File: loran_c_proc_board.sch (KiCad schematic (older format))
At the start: 0 parts

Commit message: Almost done: SPI, Relay optocouplers, ADC & DAC interface However, bug needs to be fixed: buses are not connected between hierarchical sheets
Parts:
- added BT101: Li CR2032, symbol BATTERY
- added C101: 470u 16V LowE, symbol CP1
- added C102, C105, C106, C108, C109: 100n, symbol C
- added C103, C107: 10u 6.3V Ta, symbol CP1
- added C104: 470u 6.3V, symbol CP1
- added D101: SMLVT3V3, symbol ZENER
- added FB101, FB102: Bead, symbol FILTER
- added P101: Power, symbol CONN_4X2
- added P102: Cortex SWD, symbol CONN_5X2
- added P103: Clock board, symbol CONN_5X2
- added R101: 100k, symbol R
- added R102: 33, symbol R
- added R103, R104, R105: 10, symbol R
- added R106, R107: 200, symbol R
- added U101: LD1117S33, symbol NCP1117ST33T3G
- added U102, U103: 74AC14, symbol 74HC14
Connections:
- net labels added: +15V, +5V, -15V, BPPS, BPROG, BSWD, CB_OSC, CB_PO1, CB_PO2, CB_PPS, NTRST, PPS3, PROG_OUT1, PROG_OUT2, SWCLK, SWDIO
- net labels removed: +3.3VADC, +5VA
- wire segments 0 -> 127
- no-connect marks 0 -> 4
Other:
- note added: "KEY"
- note added: "Place close to R? and P?"
- note added: "VDD"

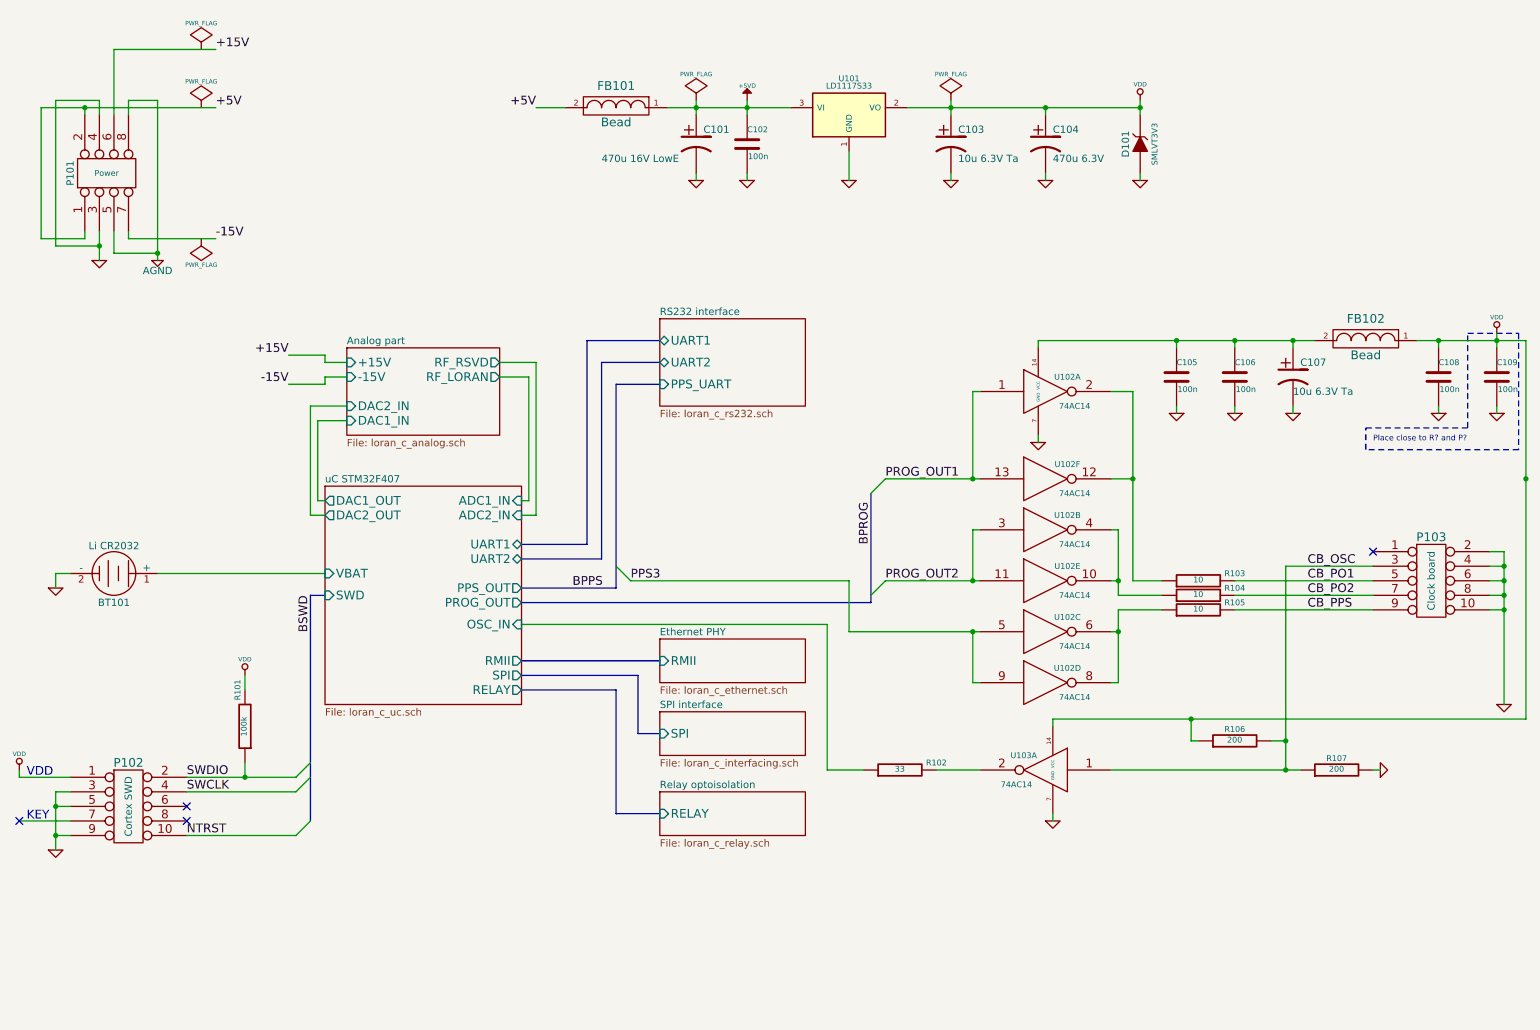
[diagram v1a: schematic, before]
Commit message: FIXED: no more buses on hierarchical sheet ports
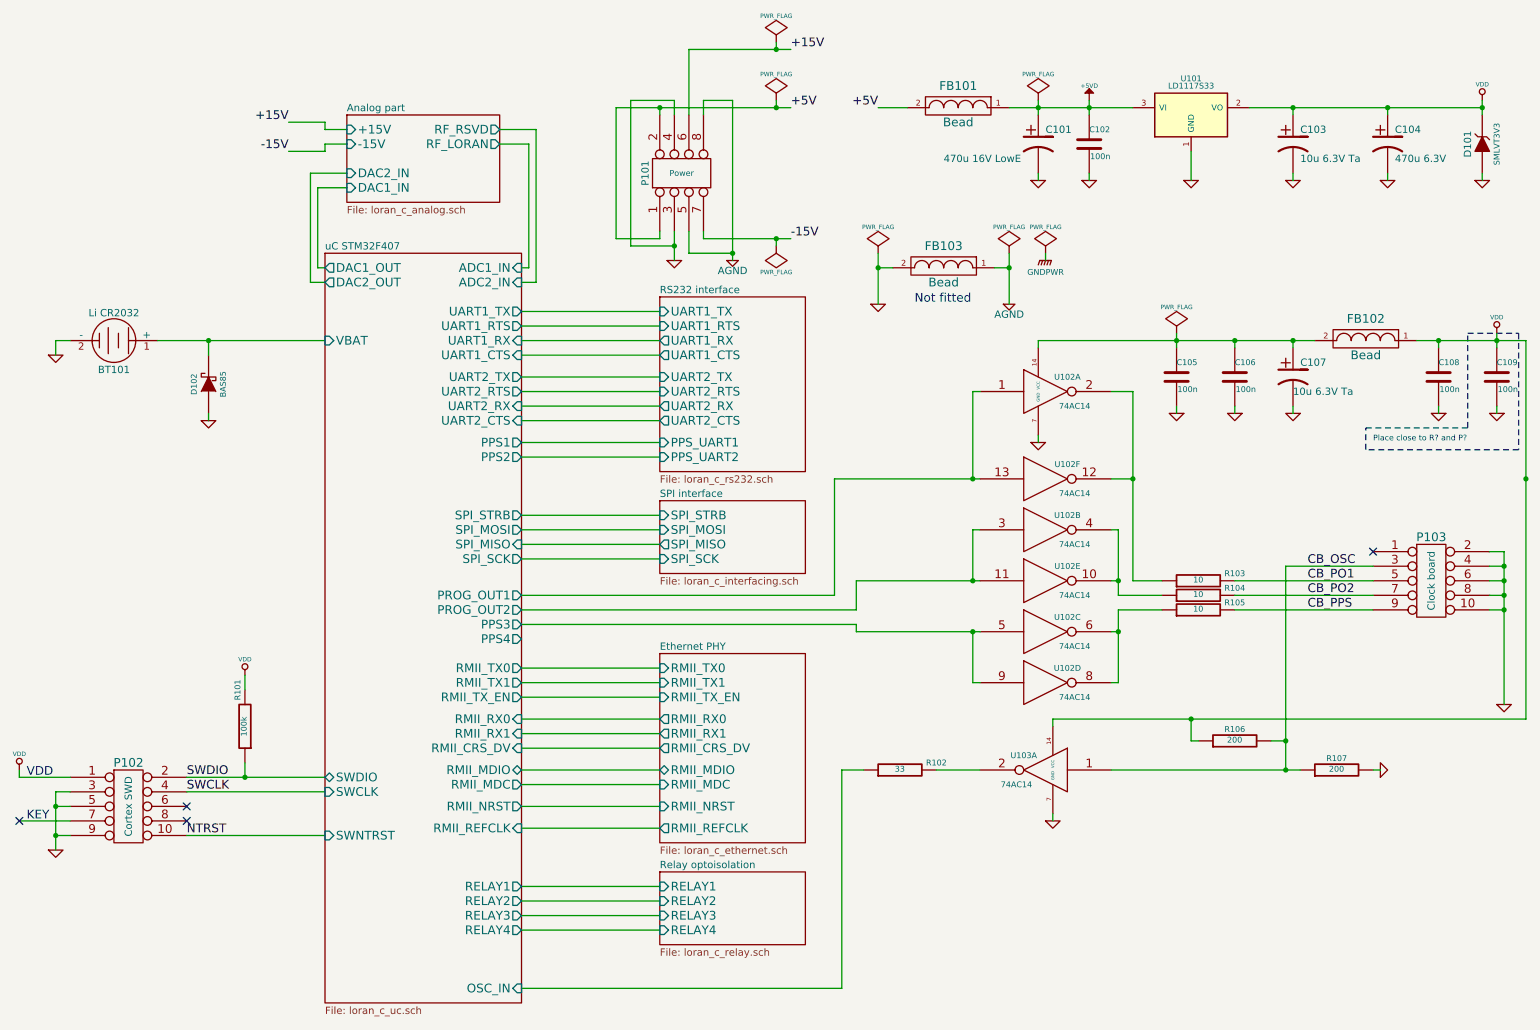
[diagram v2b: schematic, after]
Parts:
- added D102: BAS85, symbol DIODESCH
- added FB103: Bead, symbol FILTER
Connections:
- net AGND: now also FB103.1
- net GND: now also D102.1 (A), FB103.2
- net uC STM32F407/VBAT: now also D102.2 (K)
- net PPS3 renamed uC STM32F407/PPS3
- net PROG_OUT1 renamed uC STM32F407/PROG_OUT1
- net PROG_OUT2 renamed uC STM32F407/PROG_OUT2
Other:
- note added: "Not fitted"
- moved on the sheet: BT101, C101, C102, C103, C104, D101, FB101, P101, U101

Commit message: Update: fix, assign modules to components -Fix P302 incorrect connection -Assign footprints to components (not all yet) -Back-import footprints into schematic fields
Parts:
- C101: footprint (none) -> w_pth_capacitors:CP_10x12.5mm
- C102, C105, C106, C108, C109: footprint (none) -> w_smd_capacitors:c_1206
- C103, C107: footprint (none) -> w_smd_capacitors:c_tant_B
- C104: footprint (none) -> w_pth_capacitors:CP_6.3x11mm
- D101: footprint (none) -> w_smd_diode:do214aa
- D102: footprint (none) -> w_smd_diode:sod80c
- FB101, FB102, FB103: footprint (none) -> w_pth_resistors:RC07
- P102, P103: footprint (none) -> w_conn_strip:vasch_strip_5x2
- R101, R102, R103, R104, R105, R106, R107: footprint (none) -> w_smd_resistors:r_1206
- U101: footprint (none) -> SMD_Packages:SOT223
- U102, U103: footprint (none) -> w_smd_dil:so-16
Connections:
- net CB_OSC: now also R107.2; no longer R107.1
- net GND: now also R107.1; no longer R107.2
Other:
- note removed: "Place close to R? and P?"
- moved on the sheet: C109, R102, R106, R107, U103A

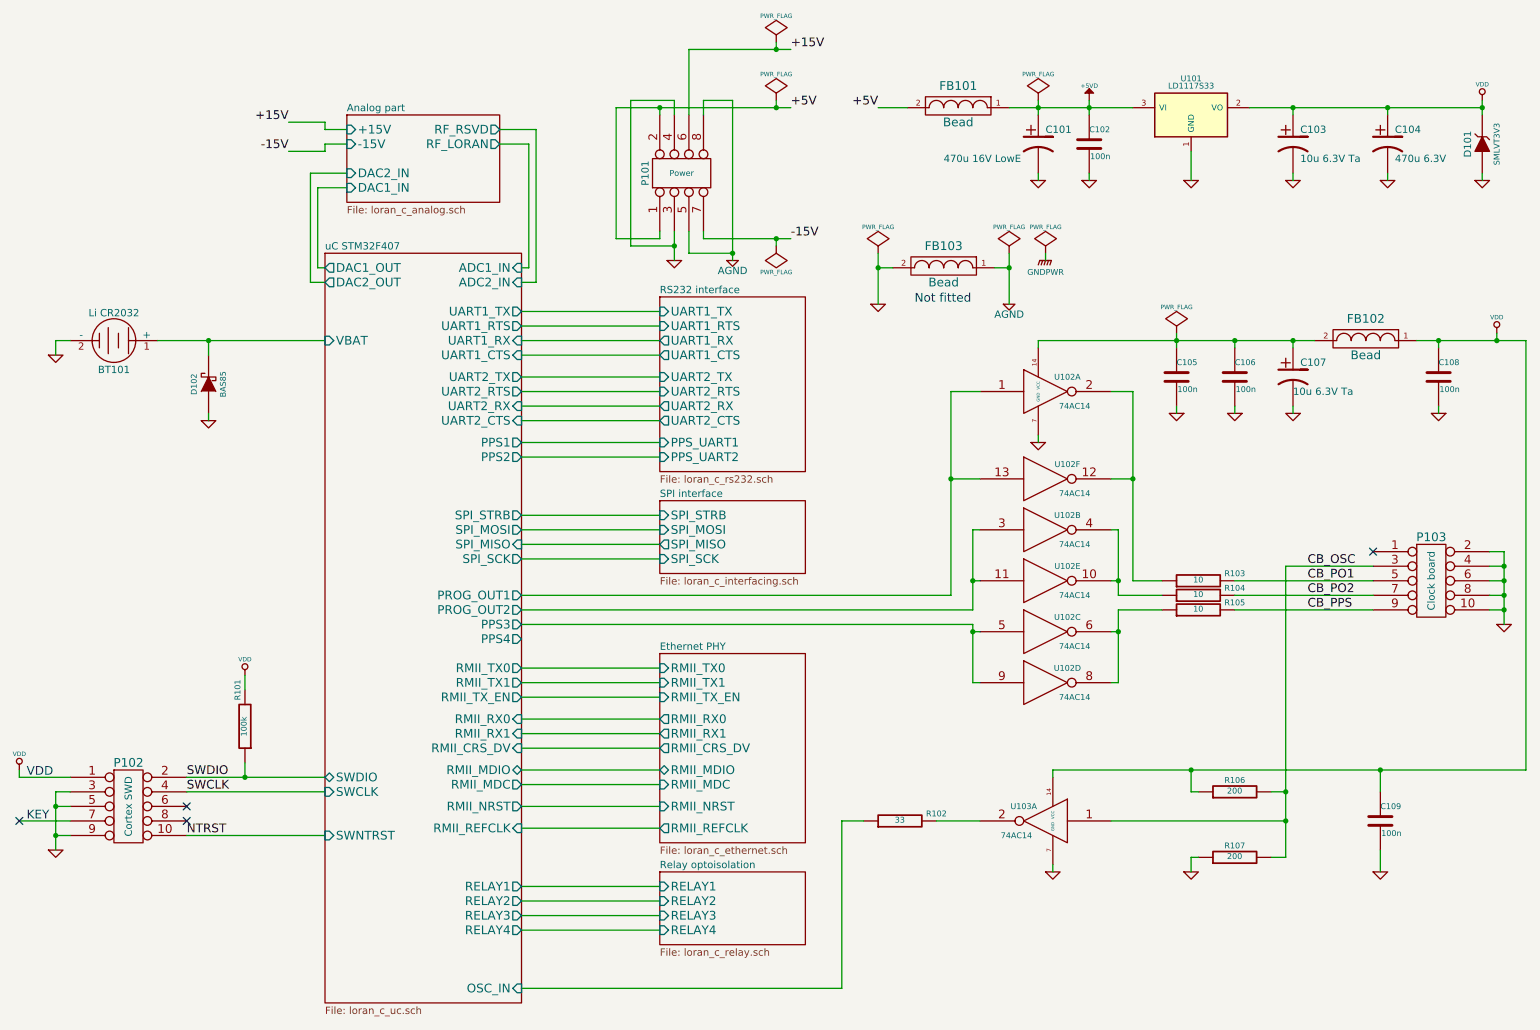
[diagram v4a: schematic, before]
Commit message: Update: assign footprint to P101, fix mounting hole symbol (pin # missing)
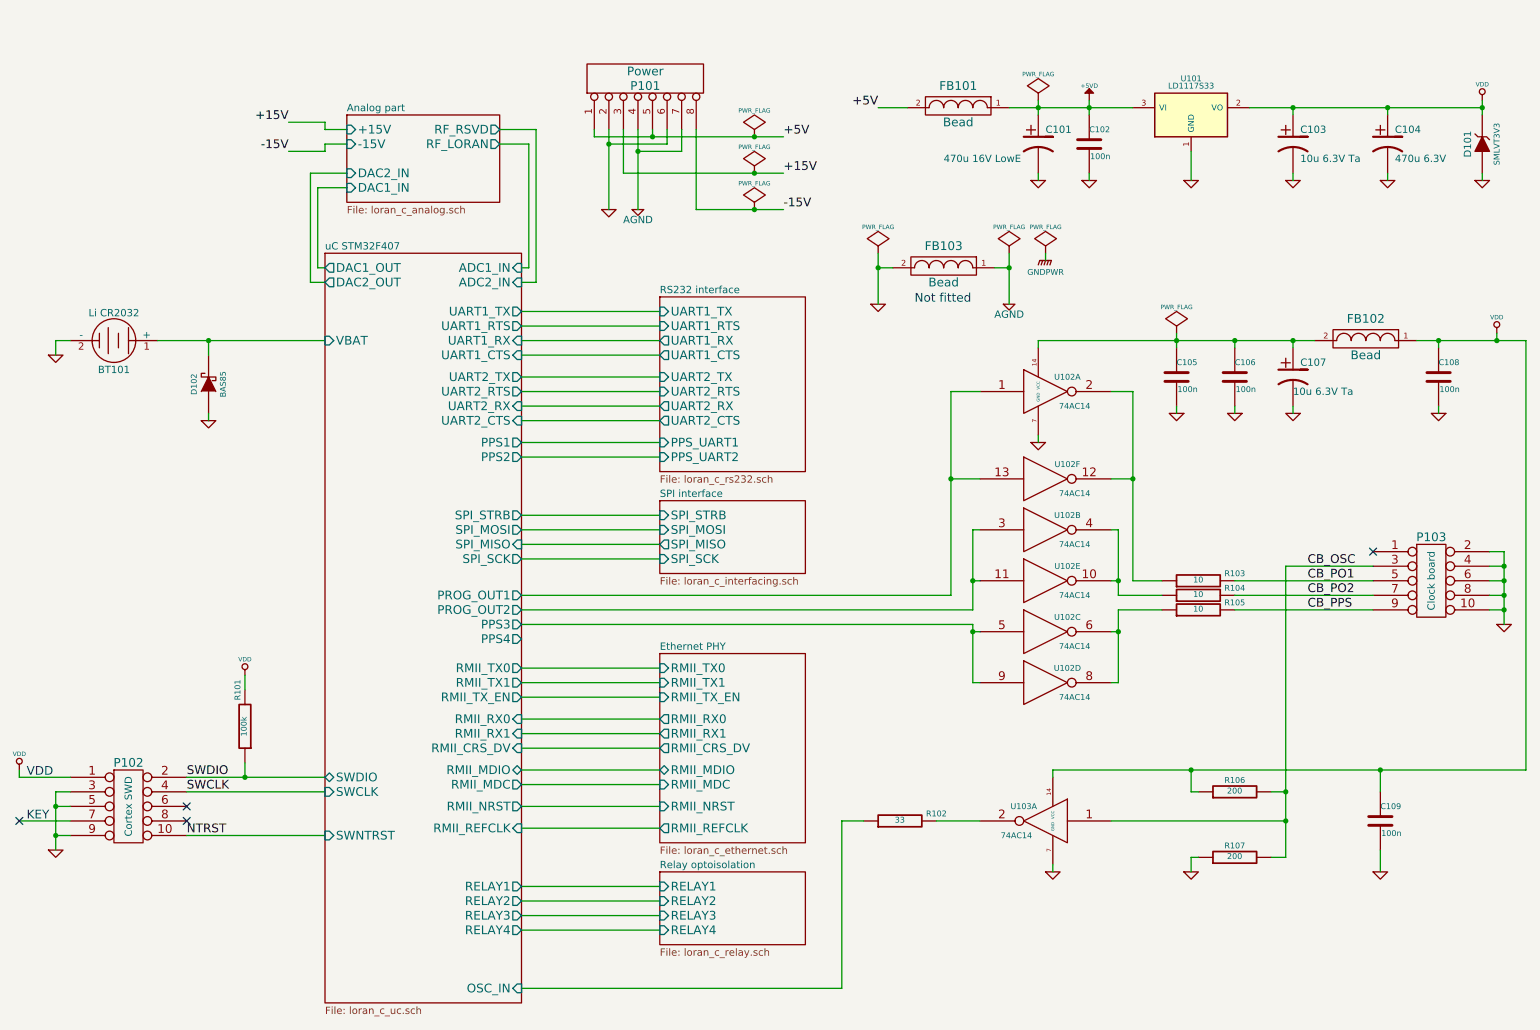
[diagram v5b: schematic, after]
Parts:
- removed P101: Power, symbol CONN_4X2
- added P101: Power, symbol CONN_8
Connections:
- net +15V: now also P101.3 (P3)
- net +5V: now also P101.1 (P1), P101.5 (P5)
- net -15V: now also P101.8 (P8)
- net AGND: now also P101.4 (P4), P101.7 (P7)
- net GND: now also P101.2 (P2), P101.6 (P6)

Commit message: Update: minor schematic rework (due to PCB routing), PCB routing in early stage
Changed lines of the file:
@@
 	8250 4750 8300 4750
 Wire Wire Line
-	8300 4600 8300 4750
-Wire Wire Line
-	8300 4750 8300 5100
+	8300 4600 8300 5100
 Wire Wire Line
 	8300 5100 8250 5100
@@
 	8250 4050 8300 4050
 Wire Wire Line
-	8300 4050 8300 4400
-Wire Wire Line
-	8300 4400 8300 4500
+	8300 4050 8300 4500
 Wire Wire Line
 	8300 4400 8250 4400
@@
 	8250 3100 8400 3100
 Wire Wire Line
-	8400 3100 8400 3700
-Wire Wire Line
-	8400 3700 8400 4400
+	8400 3100 8400 4400
 Wire Wire Line
 	8400 3700 8250 3700
@@
 	7350 4050 7300 4050
 Wire Wire Line
-	7300 4050 7300 4400
-Wire Wire Line
-	7300 4400 7300 4600
+	7300 4050 7300 4600
 Wire Wire Line
 	7300 4400 7350 4400
@@
 	7300 4750 7350 4750
 Wire Wire Line
-	7300 4700 7300 4750
-Wire Wire Line
-	7300 4750 7300 5100
+	7300 4700 7300 5100
 Wire Wire Line
 	7300 5100 7350 5100
@@
 	7750 2750 7750 2800
 Wire Wire Line
-	10350 2750 10500 2750
-Wire Wire Line
-	10500 2750 10900 2750
-Wire Wire Line
-	10900 2750 11100 2750
+	10350 2750 11100 2750
 Connection ~ 10900 2750
 Wire Wire Line
-	7750 2750 8700 2750
-Wire Wire Line
-	8700 2750 9100 2750
-Wire Wire Line
-	9100 2750 9500 2750
-Wire Wire Line
-	9500 2750 9650 2750
+	7750 2750 9650 2750
 Wire Wire Line
 	9500 2750 9500 2800
@@
 	10500 3200 10500 3250
 Wire Wire Line
-	10950 4200 10950 4300
-Wire Wire Line
-	10950 4300 10950 4400
-Wire Wire Line
-	10950 4400 10950 4500
-Wire Wire Line
-	10950 4500 10950 4600
-Wire Wire Line
-	10950 4600 10950 4700
+	10950 4200 10950 4700
 Wire Wire Line
 	11100 2750 11100 5700
@@
 	1100 5850 1000 5850
 Wire Wire Line
-	1000 5850 1000 5950
-Wire Wire Line
-	1000 5950 1000 6150
-Wire Wire Line
-	1000 6150 1000 6250
+	1000 5850 1000 6250
 Wire Wire Line
 	1100 5950 1000 5950
@@
 	6650 1150 6850 1150
 Wire Wire Line
-	7550 1150 7750 1150
-Wire Wire Line
-	7750 1150 8100 1150
-Wire Wire Line
-	8100 1150 8400 1150
-Wire Wire Line
-	7750 1100 7750 1150
-Wire Wire Line
-	7750 1150 7750 1200
-Wire Wire Line
-	8100 1100 8100 1150
-Wire Wire Line
-	8100 1150 8100 1200
+	7550 1150 8400 1150
+Wire Wire Line
+	7750 1100 7750 1200
+Wire Wire Line
+	8100 1100 8100 1200
 Connection ~ 7750 1150
 Wire Wire Line
@@
 Connection ~ 8100 1150
 Wire Wire Line
-	9200 1150 9500 1150
-Wire Wire Line
-	9500 1150 10150 1150
-Wire Wire Line
-	10150 1150 10800 1150
-Wire Wire Line
-	10800 1100 10800 1150
-Wire Wire Line
-	10800 1150 10800 1200
+	9200 1150 10800 1150
+Wire Wire Line
+	10800 1100 10800 1200
 Connection ~ 9500 1150
 Wire Wire Line
@@
 	4300 2350 4200 2350
 Wire Wire Line
-	8700 2700 8700 2750
-Wire Wire Line
-	8700 2750 8700 2800
+	8700 2700 8700 2800
 Wire Wire Line
 	7850 5750 7850 5700
 Wire Wire Line
-	7850 5700 8800 5700
-Wire Wire Line
-	8800 5700 10100 5700
-Wire Wire Line
-	10100 5700 11100 5700
+	7850 5700 11100 5700
 Connection ~ 9450 6050
 Wire Wire Line
 	9450 4300 10050 4300
 Wire Wire Line
-	9450 4300 9450 5850
-Wire Wire Line
-	9450 5850 9450 6050
-Wire Wire Line
-	9450 6050 9450 6300
+	9450 4300 9450 6300
 Wire Wire Line
 	8850 5850 8800 5850
@@
 	7150 4500 4200 4500
 Wire Wire Line
-	7150 3100 7150 3700
-Wire Wire Line
-	7150 3700 7150 4500
+	7150 3100 7150 4500
 Wire Wire Line
 	7300 4600 4200 4600
@@
 	4200 4700 7300 4700
 Wire Wire Line
-	1900 5750 2300 5750
-Wire Wire Line
-	2300 5750 2850 5750
+	1900 5750 2850 5750
 Wire Wire Line
 	2850 5850 1900 5850
@@
 	1900 6150 2850 6150
 Wire Wire Line
-	1700 2750 2050 2750
-Wire Wire Line
-	2050 2750 2850 2750
+	1700 2750 2850 2750
 $Comp
 L PWR_FLAG #FLG028
@@
 $EndComp
 Wire Wire Line
-	6650 2150 6650 2250
-Wire Wire Line
-	6650 2250 6650 2500
-Wire Wire Line
-	7550 2150 7550 2250
-Wire Wire Line
-	7550 2250 7550 2500
+	6650 2150 6650 2500
+Wire Wire Line
+	7550 2150 7550 2500
 $Comp
 L PWR_FLAG #FLG031
@@
 	4700 1300 4700 1350
 Wire Wire Line
-	4700 1350 5100 1350
-Wire Wire Line
-	5100 1350 5800 1350
-Wire Wire Line
-	5800 1350 6000 1350
+	4700 1350 6000 1350
 Wire Wire Line
 	5100 1350 5100 1300
 Wire Wire Line
-	4800 1300 4800 1400
-Wire Wire Line
-	4800 1400 4800 1850
+	4800 1300 4800 1850
 Wire Wire Line
 	4800 1400 5200 1400
@@
 	5200 1400 5200 1300
 Wire Wire Line
-	5000 1300 5000 1450
-Wire Wire Line
-	5000 1450 5000 1850
+	5000 1300 5000 1850
 Wire Wire Line
 	5000 1450 5300 1450
@@
 	4900 1300 4900 1600
 Wire Wire Line
-	4900 1600 5800 1600
-Wire Wire Line
-	5800 1600 6000 1600
+	4900 1600 6000 1600
 Wire Wire Line
 	5400 1300 5400 1850
 Wire Wire Line
-	5400 1850 5800 1850
-Wire Wire Line
-	5800 1850 6000 1850
+	5400 1850 6000 1850
 Connection ~ 5800 1350
 Connection ~ 5800 1600
